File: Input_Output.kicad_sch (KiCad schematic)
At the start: 19 parts, among them J1 Conn_01x04, J13 Conn_ARM_SWD_TagConnect_TC203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, J14 Conn_01x06, J2 Conn_01x06, J3 Conn_01x02, J7 Conn_01x05, J8 USB_B_Micro, J9 Conn_ARM_SWD_TagConnect_TC203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, U32 Micro_SD_Card_Det1

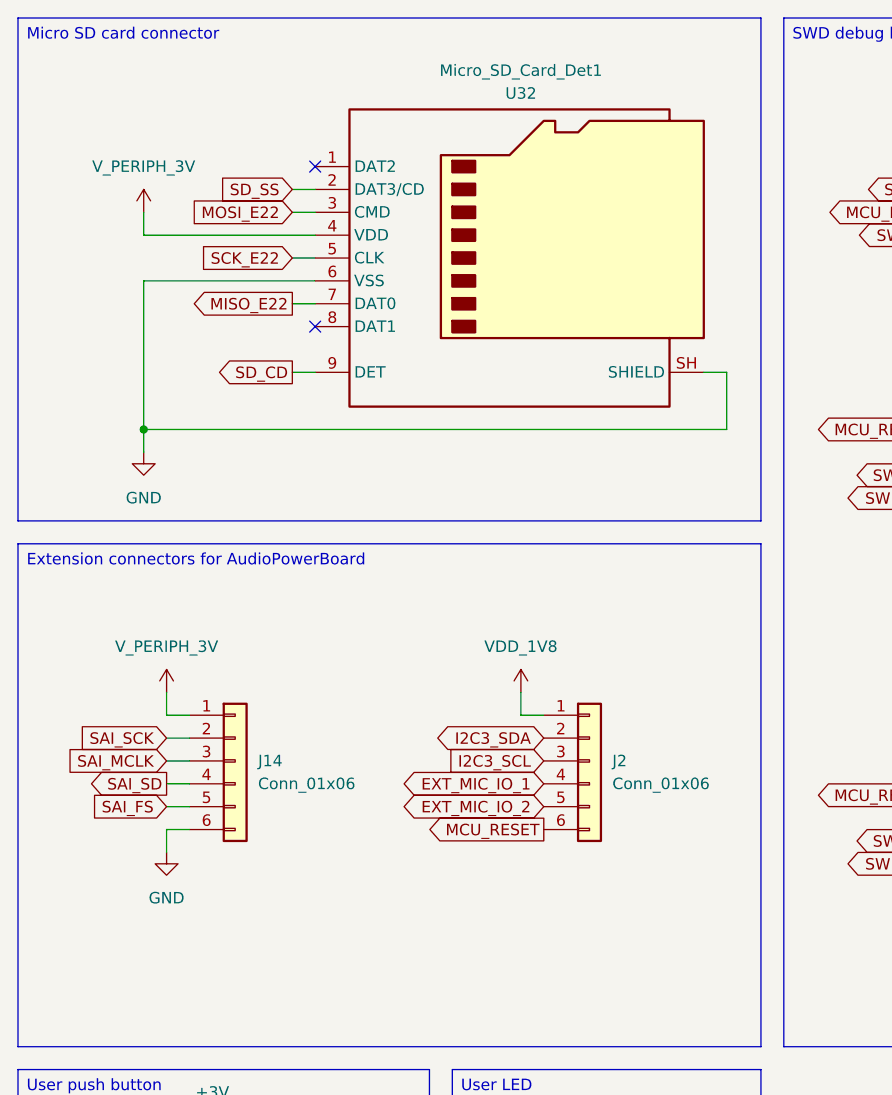
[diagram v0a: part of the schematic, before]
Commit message: PCB component placement according to AIoT2
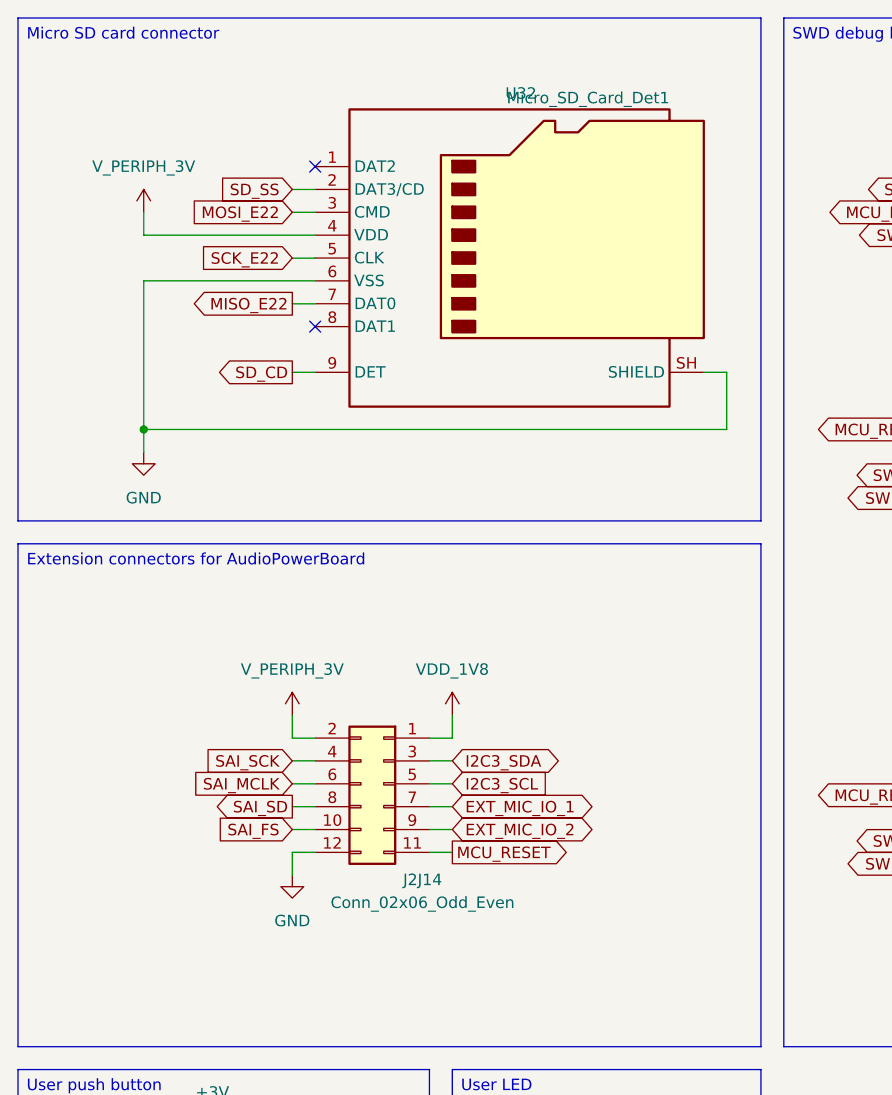
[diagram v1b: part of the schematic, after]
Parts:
- removed J14, J2: Conn_01x06, Connector_PinHeader_2.54mm:PinHeader_1x06_P2.54mm_Vertical, symbol Connector_Generic:Conn_01x06
- added J2J14: Conn_02x06_Odd_Even, Connector_PinHeader_2.54mm:PinHeader_2x06_P2.54mm_Vertical, symbol Connector_Generic:Conn_02x06_Odd_Even
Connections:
- net EXT_MIC_IO_1: now also J2J14.7 (Pin_7)
- net EXT_MIC_IO_2: now also J2J14.9 (Pin_9)
- net GND: now also J2J14.12 (Pin_12)
- net I2C3_SCL: now also J2J14.5 (Pin_5)
- net I2C3_SDA: now also J2J14.3 (Pin_3)
- net MCU_RESET: now also J2J14.11 (Pin_11)
- net SAI_FS: now also J2J14.10 (Pin_10)
- net SAI_MCLK: now also J2J14.6 (Pin_6)
- net SAI_SCK: now also J2J14.4 (Pin_4)
- net SAI_SD: now also J2J14.8 (Pin_8)
- net VDD_1V8: now also J2J14.1 (Pin_1)
- net V_PERIPH_3V: now also J2J14.2 (Pin_2)

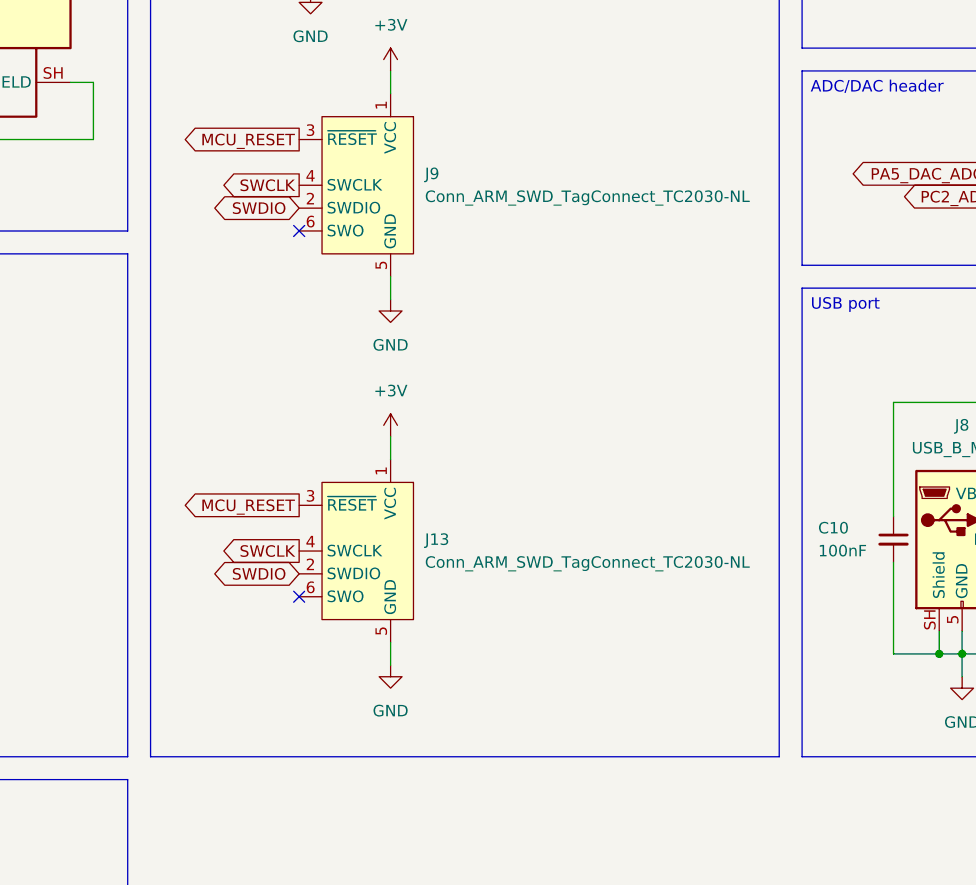
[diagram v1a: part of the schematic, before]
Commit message: pcb: start 2-layer routing
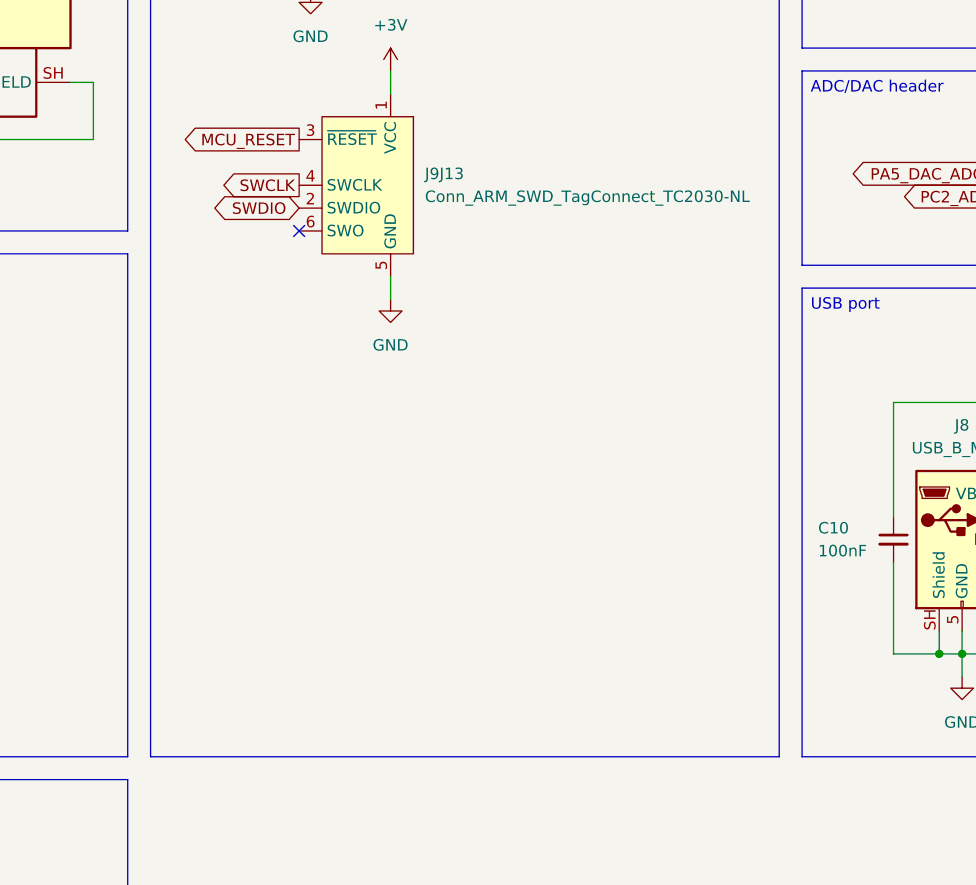
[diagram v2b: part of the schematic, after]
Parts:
- removed J13: Conn_ARM_SWD_TagConnect_TC2030-NL, Connector:Tag-Connect_TC2030-IDC-NL_2x03_P1.27mm_Vertical, symbol Connector:Conn_ARM_SWD_TagConnect_TC2030-NL
- J9J13: renamed from J9; footprint Connector:Tag-Connect_TC2030-IDC-NL_2x03_P1.27mm_Vertical -> footprints:Tag-Connect_TC2030-IDC-NL_2x03_P1.27mm_Vertical_TopBottom
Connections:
- no-connect marks 5 -> 4

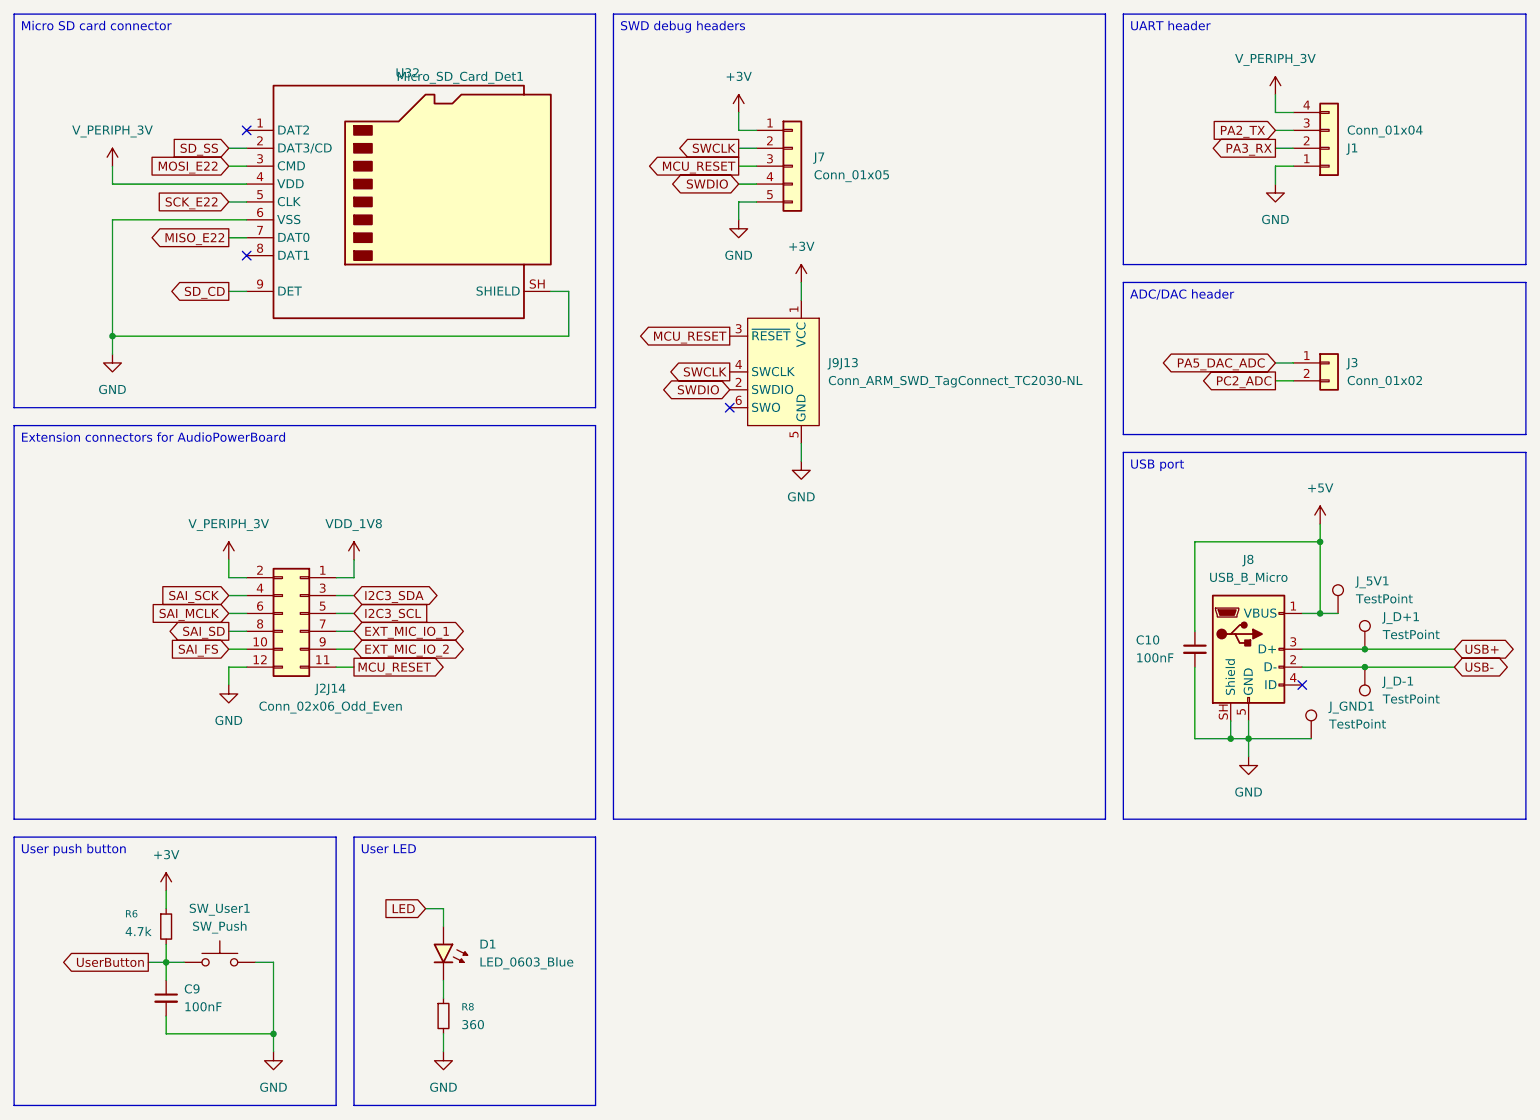
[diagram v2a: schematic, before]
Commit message: schematics: add some DNP for Ambient variant
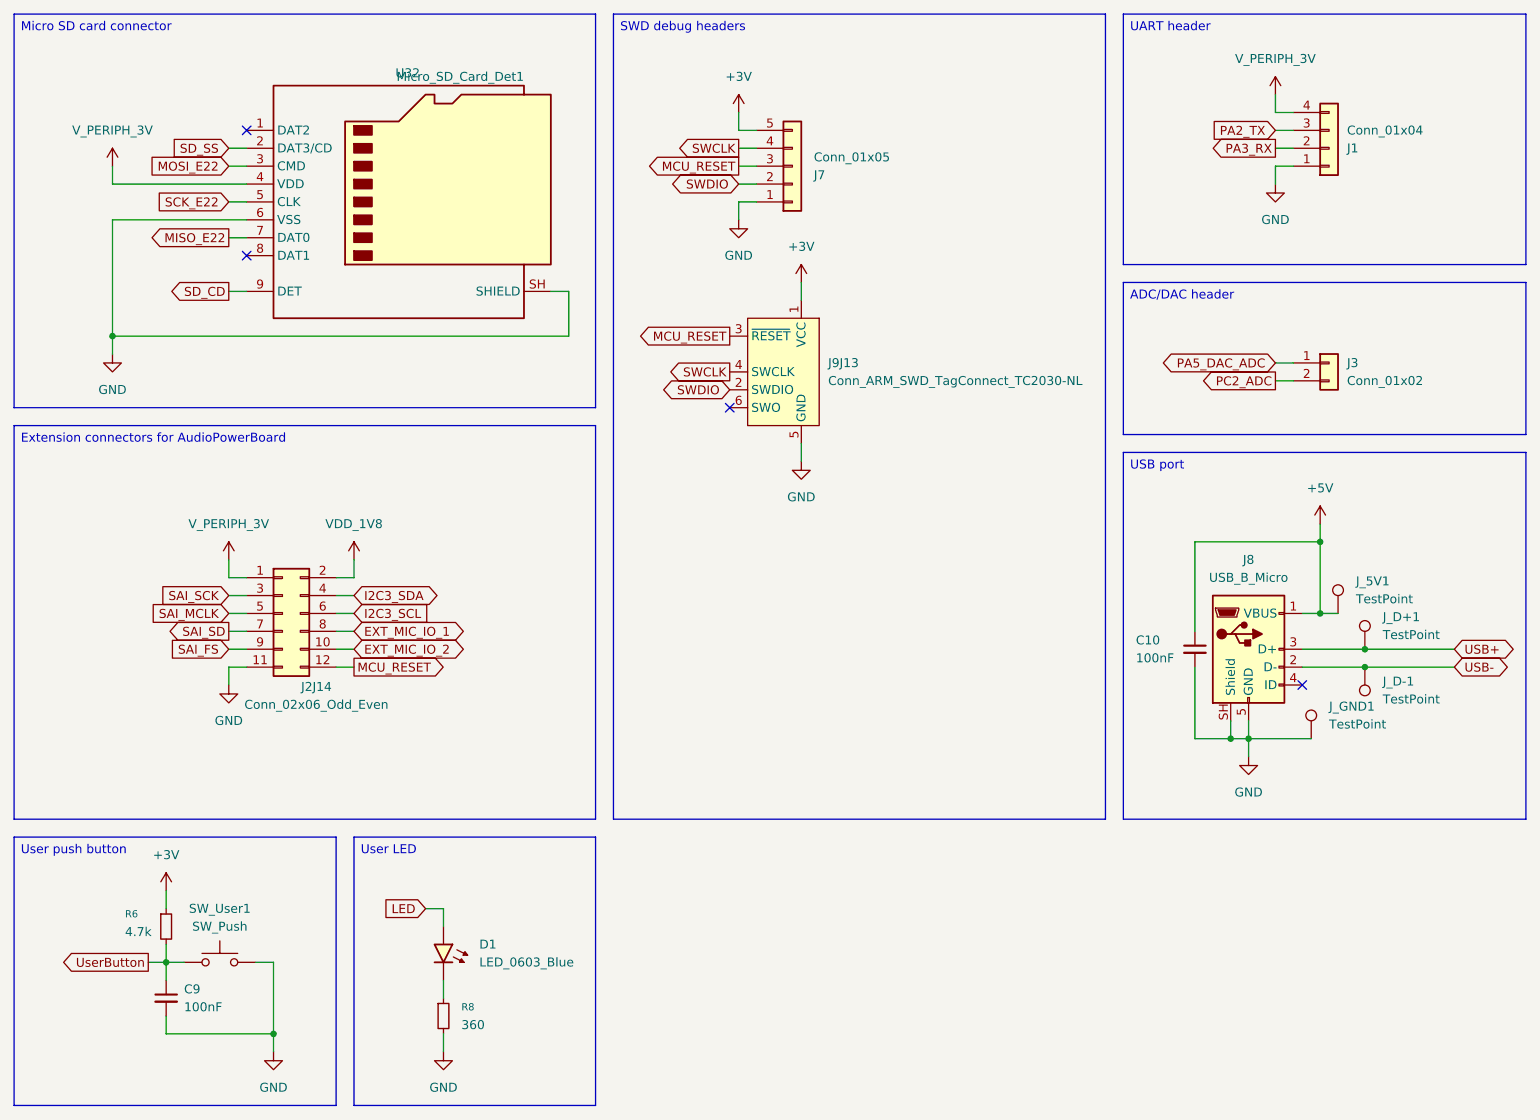
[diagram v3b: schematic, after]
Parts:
- J2J14: footprint Connector_PinHeader_2.54mm:PinHeader_2x06_P2.54mm_Vertical -> Connector_PinSocket_2.54mm:PinSocket_2x06_P2.54mm_Vertical
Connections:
- net +3V: now also J7.5 (Pin_5); no longer J7.1 (Pin_1)
- net EXT_MIC_IO_1: now also J2J14.8 (Pin_8); no longer J2J14.7 (Pin_7)
- net EXT_MIC_IO_2: now also J2J14.10 (Pin_10); no longer J2J14.9 (Pin_9)
- net GND: now also J2J14.11 (Pin_11), J7.1 (Pin_1); no longer J2J14.12 (Pin_12), J7.5 (Pin_5)
- net I2C3_SCL: now also J2J14.6 (Pin_6); no longer J2J14.5 (Pin_5)
- net I2C3_SDA: now also J2J14.4 (Pin_4); no longer J2J14.3 (Pin_3)
- net MCU_RESET: now also J2J14.12 (Pin_12); no longer J2J14.11 (Pin_11)
- net SAI_FS: now also J2J14.9 (Pin_9); no longer J2J14.10 (Pin_10)
- net SAI_MCLK: now also J2J14.5 (Pin_5); no longer J2J14.6 (Pin_6)
- net SAI_SCK: now also J2J14.3 (Pin_3); no longer J2J14.4 (Pin_4)
- net SAI_SD: now also J2J14.7 (Pin_7); no longer J2J14.8 (Pin_8)
- net SWCLK: now also J7.4 (Pin_4); no longer J7.2 (Pin_2)
- net SWDIO: now also J7.2 (Pin_2); no longer J7.4 (Pin_4)
- net VDD_1V8: now also J2J14.2 (Pin_2); no longer J2J14.1 (Pin_1)
- net V_PERIPH_3V: now also J2J14.1 (Pin_1); no longer J2J14.2 (Pin_2)
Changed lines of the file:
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@@
-	)
-	(symbol
-		(lib_id "Connector_Generic:Conn_02x06_Odd_Even")
-		(at 71.12 118.11 0)
-		(mirror y)
-		(unit 1)
-		(body_style 1)
-		(exclude_from_sim no)
-		(in_bom yes)
-		(on_board yes)
-		(in_pos_files yes)
-		(dnp no)
-		(property "Reference" "J2J14"
-			(at 75.438 128.778 0)
-			(show_name no)
-			(do_not_autoplace no)
-			(effects
-				(font
-					(size 1.27 1.27)
-				)
-			)
-		)
-		(property "Value" "Conn_02x06_Odd_Even"
-			(at 75.438 131.318 0)
-			(show_name no)
-			(do_not_autoplace no)
-			(effects
-				(font
-					(size 1.27 1.27)
-				)
-			)
-		)
-		(property "Footprint" "Connector_PinHeader_2.54mm:PinHeader_2x06_P2.54mm_Vertical"
-			(at 71.12 118.11 0)
-			(hide yes)
-			(show_name no)
-			(do_not_autoplace no)
-			(effects
-				(font
-					(size 1.27 1.27)
-				)
-			)
-		)
-		(property "Datasheet" ""
-			(at 71.12 118.11 0)
-			(hide yes)
-			(show_name no)
-			(do_not_autoplace no)
-			(effects
-				(font
-					(size 1.27 1.27)
-				)
-			)
-		)
-		(property "Description" "Generic connector, double row, 02x06, odd/even pin numbering scheme (row 1 odd numbers, row 2 even numbers), script generated (kicad-library-utils/schlib/autogen/connector/)"
-			(at 71.12 118.11 0)
-			(hide yes)
-			(show_name no)
-			(do_not_autoplace no)
-			(effects
-				(font
-					(size 1.27 1.27)
-				)
-			)
-		)
-		(pin "2"
-		)
-		(pin "6"
-		)
-		(pin "4"
-		)
-		(pin "3"
-		)
-		(pin "9"
-		)
-		(pin "10"
-		)
-		(pin "1"
-		)
-		(pin "12"
-		)
-		(pin "7"
-		)
-		(pin "5"
-		)
-		(pin "8"
-		)
-		(pin "11"
-		)
-		(instances
-			(project "uca-dkaiot2-kicad"
-				(path "/13b7de53-ecff-4b32-b513-b5b471d022a3/e21f4090-1137-445d-beac-e9326d55c77a"
-					(reference "J2J14")
-					(unit 1)
-				)
-			)
-		)
 	)
 	(symbol
@@
 					(variant
 						(name "Ambient")
+						(dnp yes)
 					)
 				)
@@
 					(variant
 						(name "Ambient")
+						(dnp yes)
 					)
 				)
@@
 	)
 	(symbol
+		(lib_id "Connector_Generic:Conn_02x06_Odd_Even")
+		(at 68.58 118.11 0)
+		(unit 1)
+		(body_style 1)
+		(exclude_from_sim no)
+		(in_bom yes)
+		(on_board yes)
+		(in_pos_files yes)
+		(dnp no)
+		(property "Reference" "J2J14"
+			(at 73.406 128.524 0)
+			(show_name no)
+			(do_not_autoplace no)
+			(effects
+				(font
+					(size 1.27 1.27)
+				)
+			)
+		)
+		(property "Value" "Conn_02x06_Odd_Even"
+			(at 73.406 131.064 0)
+			(show_name no)
+			(do_not_autoplace no)
+			(effects
+				(font
+					(size 1.27 1.27)
+				)
+			)
+		)
+		(property "Footprint" "Connector_PinSocket_2.54mm:PinSocket_2x06_P2.54mm_Vertical"
+			(at 68.58 118.11 0)
+			(hide yes)
+			(show_name no)
+			(do_not_autoplace no)
+			(effects
+				(font
+					(size 1.27 1.27)
+				)
+			)
+		)
+		(property "Datasheet" ""
+			(at 68.58 118.11 0)
+			(hide yes)
+			(show_name no)
+			(do_not_autoplace no)
+			(effects
+				(font
+					(size 1.27 1.27)
+				)
+			)
+		)
+		(property "Description" "Generic connector, double row, 02x06, odd/even pin numbering scheme (row 1 odd numbers, row 2 even numbers), script generated (kicad-library-utils/schlib/autogen/connector/)"
+			(at 68.58 118.11 0)
+			(hide yes)
+			(show_name no)
+			(do_not_autoplace no)
+			(effects
+				(font
+					(size 1.27 1.27)
+				)
+			)
+		)
+		(pin "2"
+		)
+		(pin "6"
+		)
+		(pin "4"
+		)
+		(pin "3"
+		)
+		(pin "9"
+		)
+		(pin "10"
+		)
+		(pin "1"
+		)
+		(pin "12"
+		)
+		(pin "7"
+		)
+		(pin "5"
+		)
+		(pin "8"
+		)
+		(pin "11"
+		)
+		(instances
+			(project "uca-dkaiot2-kicad"
+				(path "/13b7de53-ecff-4b32-b513-b5b471d022a3/e21f4090-1137-445d-beac-e9326d55c77a"
+					(reference "J2J14")
+					(unit 1)
+				)
+			)
+		)
+	)
+	(symbol
 		(lib_id "power:+3V0")
 		(at 44.45 54.61 0)
@@
 		(lib_id "Connector_Generic:Conn_01x05")
 		(at 140.97 54.61 0)
+		(mirror x)
 		(unit 1)
 		(body_style 1)
@@
 		(dnp no)
 		(property "Reference" "J7"
+			(at 144.018 55.88 0)
+			(show_name no)
+			(do_not_autoplace no)
+			(effects
+				(font
+					(size 1.27 1.27)
+				)
+				(justify left)
+			)
+		)
+		(property "Value" "Conn_01x05"
 			(at 144.018 53.34 0)
-			(show_name no)
-			(do_not_autoplace no)
-			(effects
-				(font
-					(size 1.27 1.27)
-				)
-				(justify left)
-			)
-		)
-		(property "Value" "Conn_01x05"
-			(at 144.018 55.88 0)
 			(show_name no)
 			(do_not_autoplace no)
@@
 					(variant
 						(name "Ambient")
+						(dnp yes)
 					)
 				)
